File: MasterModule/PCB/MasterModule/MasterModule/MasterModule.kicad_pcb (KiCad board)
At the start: 2 copper layers, 50 x 70 mm, 0 parts

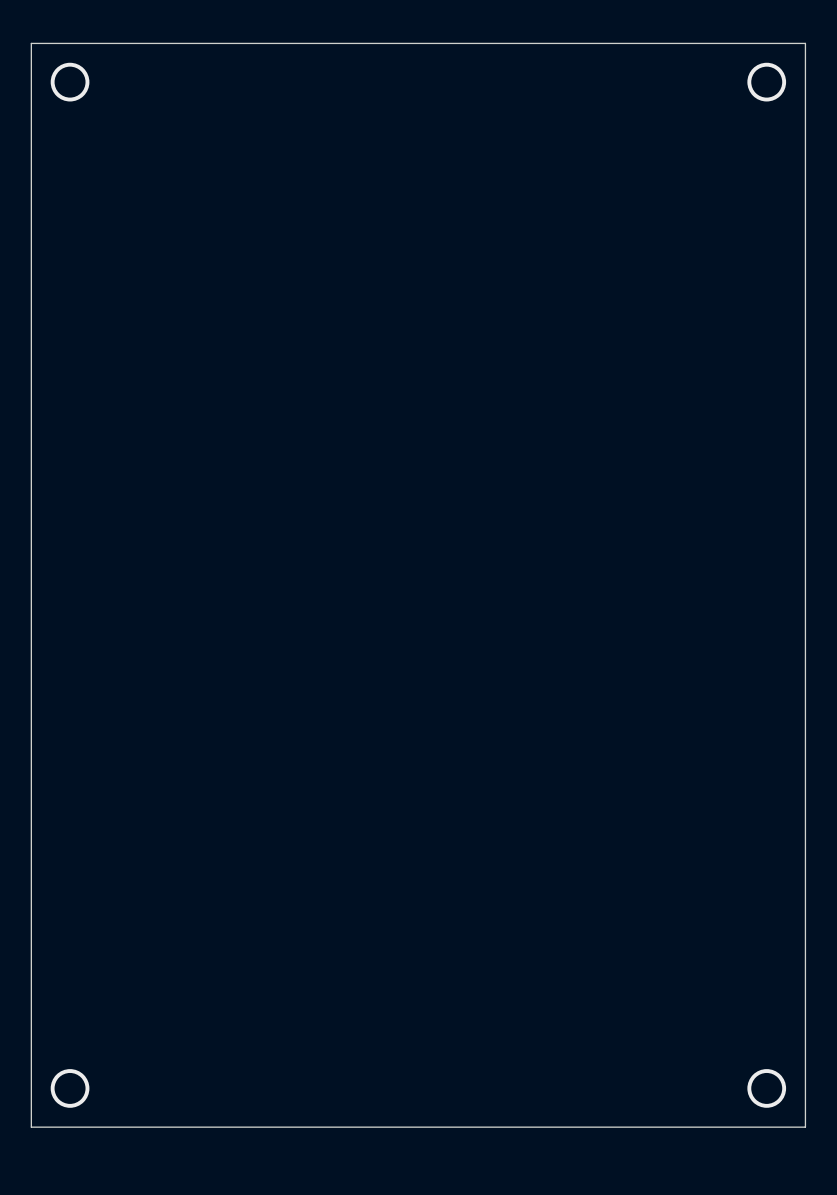
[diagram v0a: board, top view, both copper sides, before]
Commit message: [PCB][MasterModule] Create MasterModule v.1.0
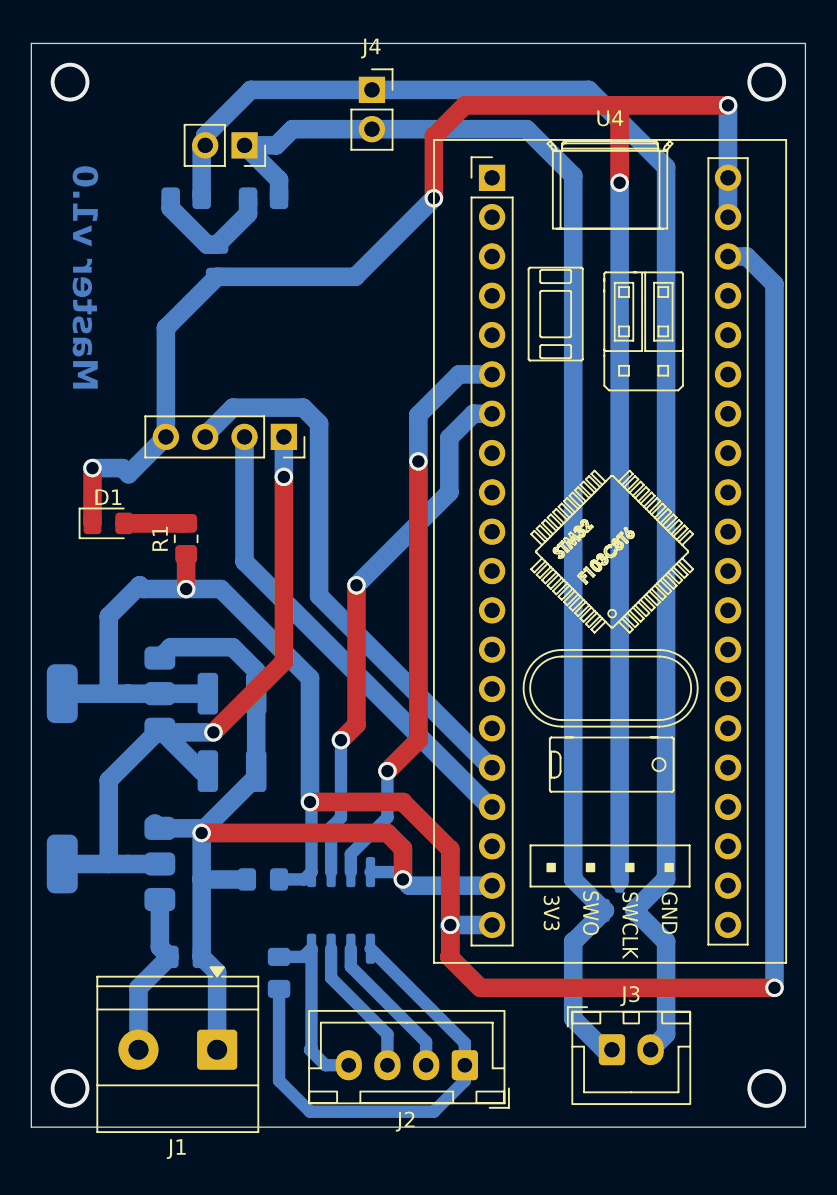
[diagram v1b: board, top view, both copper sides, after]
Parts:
- added C1: 22uF, Capacitor_SMD:C_1210_3225Metric_Pad1.33x2.70mm_HandSolder, B.Cu at (63.0, 97.0)
- added C2: 22uF, Capacitor_SMD:C_1210_3225Metric_Pad1.33x2.70mm_HandSolder, B.Cu at (63.0, 92.0)
- added C3: 10uF, Capacitor_SMD:C_0805_2012Metric_Pad1.18x1.45mm_HandSolder, B.Cu at (60.0, 109.0)
- added C4: 10uF, Capacitor_SMD:C_0805_2012Metric_Pad1.18x1.45mm_HandSolder, B.Cu at (66.0, 110.0)
- added C5: 10uF, Capacitor_SMD:C_0805_2012Metric_Pad1.18x1.45mm_HandSolder, B.Cu at (65.0, 104.0)
- added C6: 100nF, Capacitor_SMD:C_0805_2012Metric_Pad1.18x1.45mm_HandSolder, B.Cu at (62.0, 64.0)
- added D1: LED, LED_SMD:LED_0805_2012Metric_Pad1.15x1.40mm_HandSolder, F.Cu at (55.0, 81.0)
- added D2: TJA_1050_Module, MasterModuleCANFootprint:TJA1050_module, F.Cu at (62.7, 56.9)
- added D3: NUP2105L, Package_TO_SOT_SMD:SOT-23, B.Cu at (88.0, 105.1)
- added J1: Input_7V, TerminalBlock_Phoenix:TerminalBlock_Phoenix_MKDS-1,5-2-5.08_1x02_P5.08mm_Horizontal, F.Cu at (62.0, 115.0)
- added J2: UART, Connector_JST:JST_XH_B4B-XH-A_1x04_P2.50mm_Vertical, F.Cu at (78.0, 116.0)
- added J3: BUS, Connector_JST:JST_XH_B2B-XH-A_1x02_P2.50mm_Vertical, F.Cu at (87.5, 115.0)
- added J4: Diagnostic_pins, Connector_PinSocket_2.54mm:PinSocket_1x02_P2.54mm_Vertical, F.Cu at (72.0, 53.0)
- added R1: 300, Resistor_SMD:R_0805_2012Metric_Pad1.20x1.40mm_HandSolder, F.Cu at (60.0, 82.0)
- added R2: 62, Resistor_SMD:R_0805_2012Metric_Pad1.20x1.40mm_HandSolder, B.Cu at (60.0, 60.0)
- added R3: 62, Resistor_SMD:R_0805_2012Metric_Pad1.20x1.40mm_HandSolder, B.Cu at (65.0, 60.0)
- added U1: AMS1117-3.3, Package_TO_SOT_SMD:SOT-223-3_TabPin2, B.Cu at (55.1, 92.0)
- added U2: AMS1117-5.0, Package_TO_SOT_SMD:SOT-223-3_TabPin2, B.Cu at (55.1, 103.0)
- added U3: ADuM1201AR, Package_SO:SOIC-8_3.9x4.9mm_P1.27mm, B.Cu at (70.0, 106.0)
- added U4: YAAJ_BluePill, STM32:YAAJ_BluePill_1, F.Cu at (79.8, 58.7)
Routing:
- net GND: track 0.00 -> 181.8 mm, vias 0 -> 6
- net +3.3V: track 0.00 -> 138.9 mm, vias 0 -> 4
- net Net-(D2-CANH): track 0.00 -> 96.4 mm
- net Net-(D2-CANL): track 0.00 -> 86.8 mm
- net +5V: track 0.00 -> 45.1 mm, vias 0 -> 2
- net /UART_galvanic_isolation/TX: track 0.00 -> 37.3 mm, vias 0 -> 2
- net /CAN/CAN_RX: track 0.00 -> 35.5 mm
- net /UART_galvanic_isolation/RX: track 0.00 -> 34.6 mm, vias 0 -> 2
- net Net-(J2-Pin_1): track 0.00 -> 30.6 mm
- net /CAN/CAN_TX: track 0.00 -> 30.6 mm
- net Net-(J2-Pin_4): track 0.00 -> 11.8 mm
- net Net-(J1-Pin_2): track 0.00 -> 10.8 mm
- net Net-(J2-Pin_2): track 0.00 -> 9.54 mm
- net Net-(J2-Pin_3): track 0.00 -> 9.03 mm
- net Net-(C6-Pad1): track 0.00 -> 8.45 mm
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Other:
- board text added: "Master v1.0"

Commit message: [PCB][MasterModule] Manufactured master module v1.0
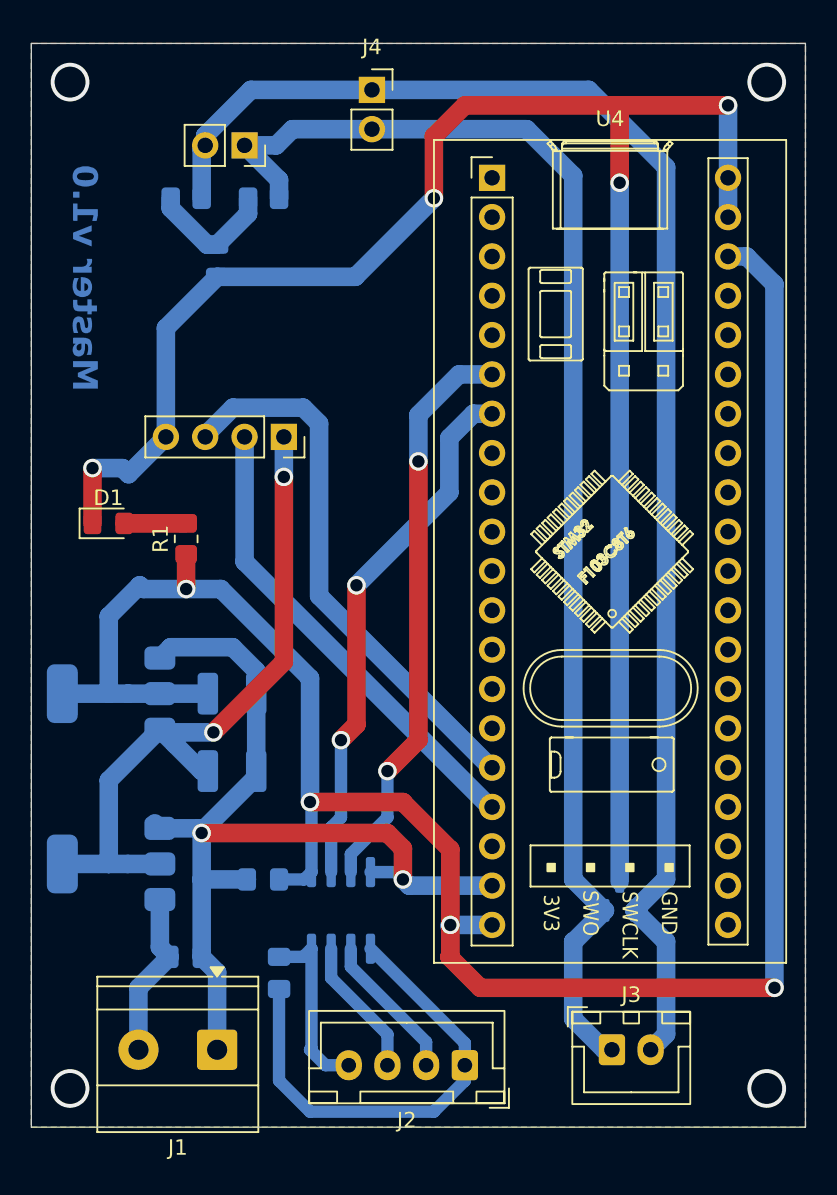
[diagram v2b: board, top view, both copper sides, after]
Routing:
- added copper zone on B.Cu, net GND
- added copper zone on F.Cu, net GND

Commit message: [PCB][MasterModule] Fix CAN transmitter to TJA1050 chip (Master v1.1)
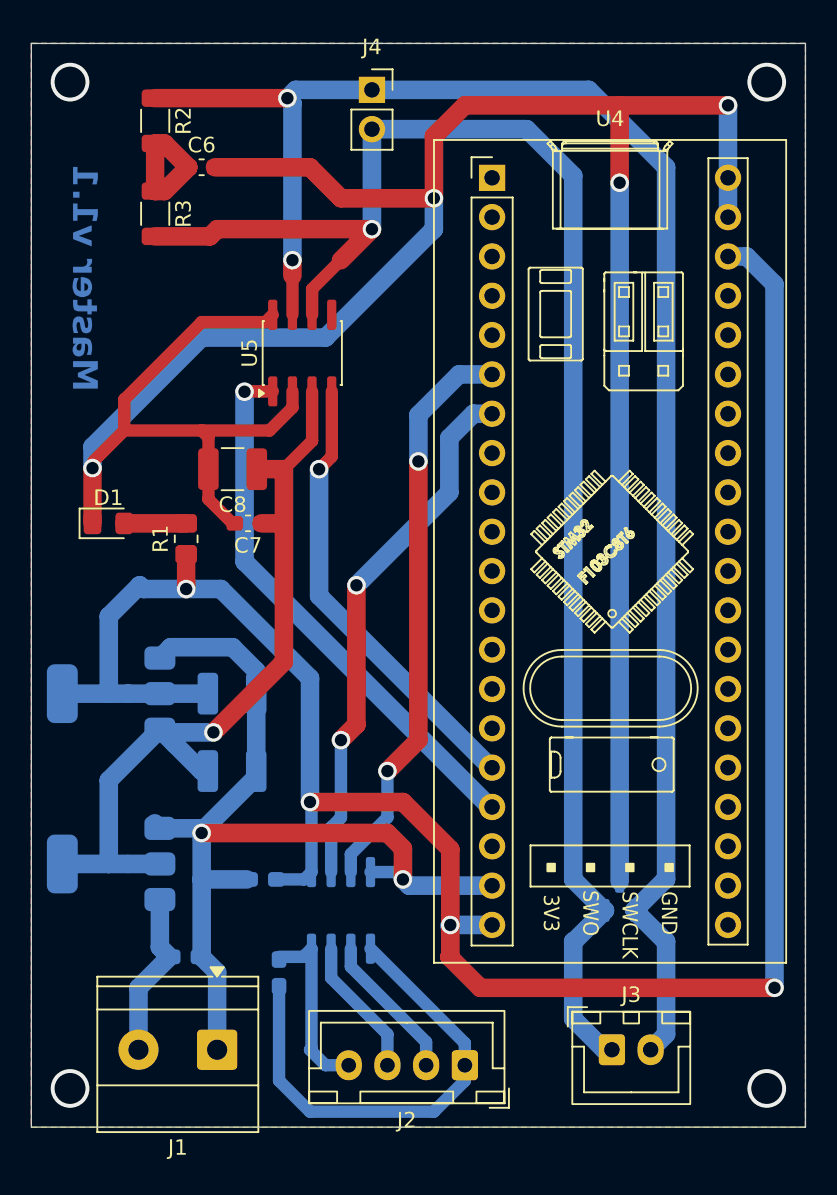
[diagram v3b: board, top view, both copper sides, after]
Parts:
- removed D2: TJA_1050_Module, MasterModuleCANFootprint:TJA1050_module
- added C7: 100nF, Capacitor_SMD:C_0603_1608Metric_Pad1.08x0.95mm_HandSolder, F.Cu at (64.0, 81.0)
- added C8: 47uF, Capacitor_SMD:C_1210_3225Metric_Pad1.33x2.70mm_HandSolder, F.Cu at (63.0, 77.5)
- added U5: TJA1051T, Package_SO:SOIC-8_3.9x4.9mm_P1.27mm, F.Cu at (67.5, 70.0)
- C3, C4, C5: footprint Capacitor_SMD:C_0805_2012Metric_Pad1.18x1.45mm_HandSolder -> Capacitor_SMD:C_0603_1608Metric_Pad1.08x0.95mm_HandSolder
- C6: footprint Capacitor_SMD:C_0805_2012Metric_Pad1.18x1.45mm_HandSolder -> Capacitor_SMD:C_0603_1608Metric_Pad1.08x0.95mm_HandSolder; moved to F.Cu
- R2, R3: footprint Resistor_SMD:R_0805_2012Metric_Pad1.20x1.40mm_HandSolder -> Resistor_SMD:R_1206_3216Metric; moved to F.Cu
- moved R3 7.07 mm to (58.0, 61.0), turned to -90 degrees
- moved C6 6.12 mm to (61.0, 58.0), turned to 0 degrees
- moved R2 5.39 mm to (58.0, 55.0), turned to -90 degrees
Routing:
- net GND: track 181.8 -> 230.4 mm
- net Net-(J3-Pin_1): track 86.8 -> 101.6 mm, vias 0 -> 1
- net Net-(J3-Pin_2): track 96.4 -> 108.7 mm, vias 0 -> 2
- net +5V: track 45.1 -> 52.0 mm, vias 2 -> 1
- net /CAN/CAN_RX: track 35.5 -> 29.3 mm, vias 0 -> 1
- net /CAN/CAN_TX: track 30.6 -> 35.4 mm, vias 0 -> 1
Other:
- board text added: "Master v1.1"
- board text removed: "Master v1.0"
